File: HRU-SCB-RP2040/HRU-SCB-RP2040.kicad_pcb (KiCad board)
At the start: 2 copper layers, 42 x 55 mm, 52 parts, among them J1 Conn_01x03_Pin, J10 Conn_01x03_Pin, J11 Conn_01x03_Pin, J12 Conn_01x03_Pin, J13 Conn_01x03_Pin, J14 Conn_01x03_Pin, J15 Conn_01x03_Pin, J16 Conn_01x03_Pin, J17 Conn_01x03_Pin, J18 Conn_01x03_Pin, J19 Conn_01x03_Pin, J2 Conn_01x03_Pin, J20 Conn_01x03_Pin, J21 Conn_01x03_Pin, J22 Conn_01x03_Pin, J23 Conn_01x03_Pin, J24 Conn_01x03_Pin, J25 Conn_01x02_Pin, J26 Pico_Socket_A, J27 Pico_Socket_B, J28 Conn_01x04_Pin, J3 Conn_01x03_Pin, J4 Conn_01x03_Pin, J5 Conn_01x03_Pin, J6 Conn_01x03_Pin, J7 Conn_01x03_Pin, J8 Conn_01x03_Pin, J9 Conn_01x03_Pin, Q1 NchFET, Q2 NchFET, U2 MAX485E, U3 MAX485E, U4 NJM7805FA

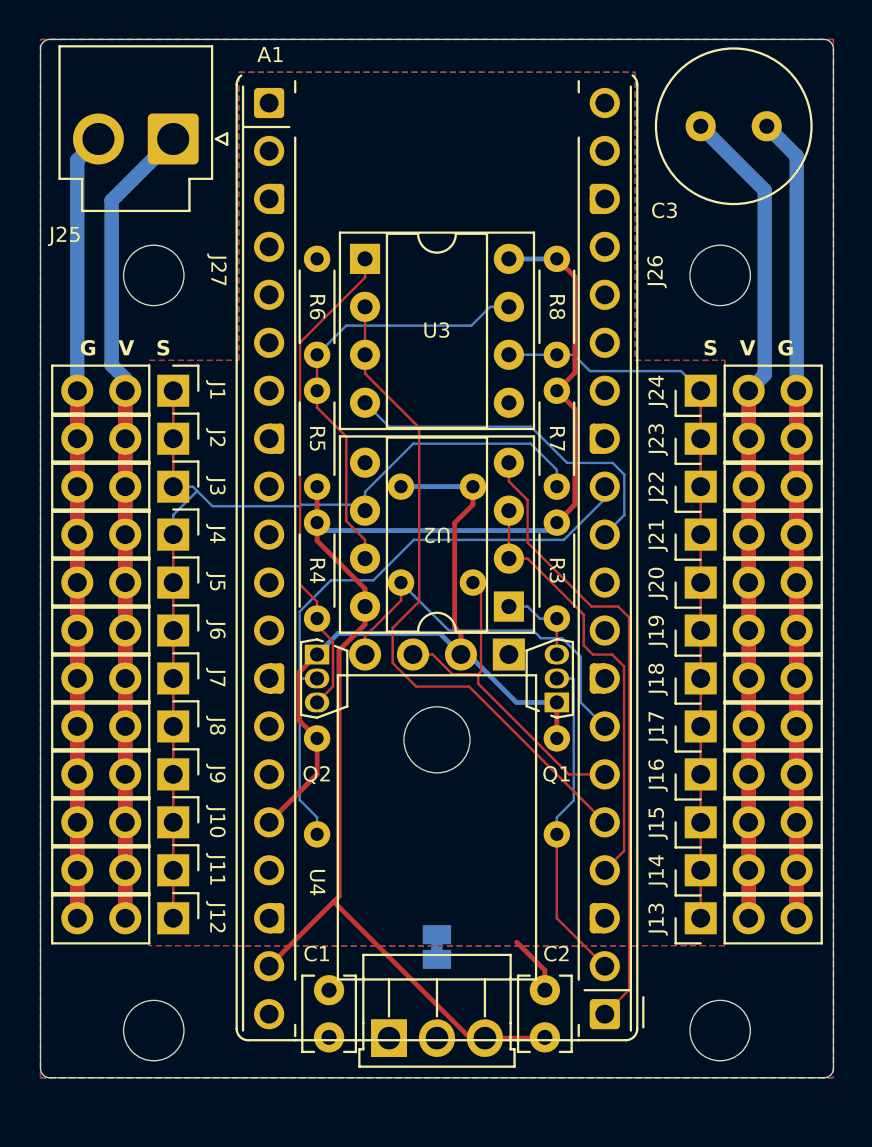
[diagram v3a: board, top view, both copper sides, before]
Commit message: Modify footprint of the registers and regulators
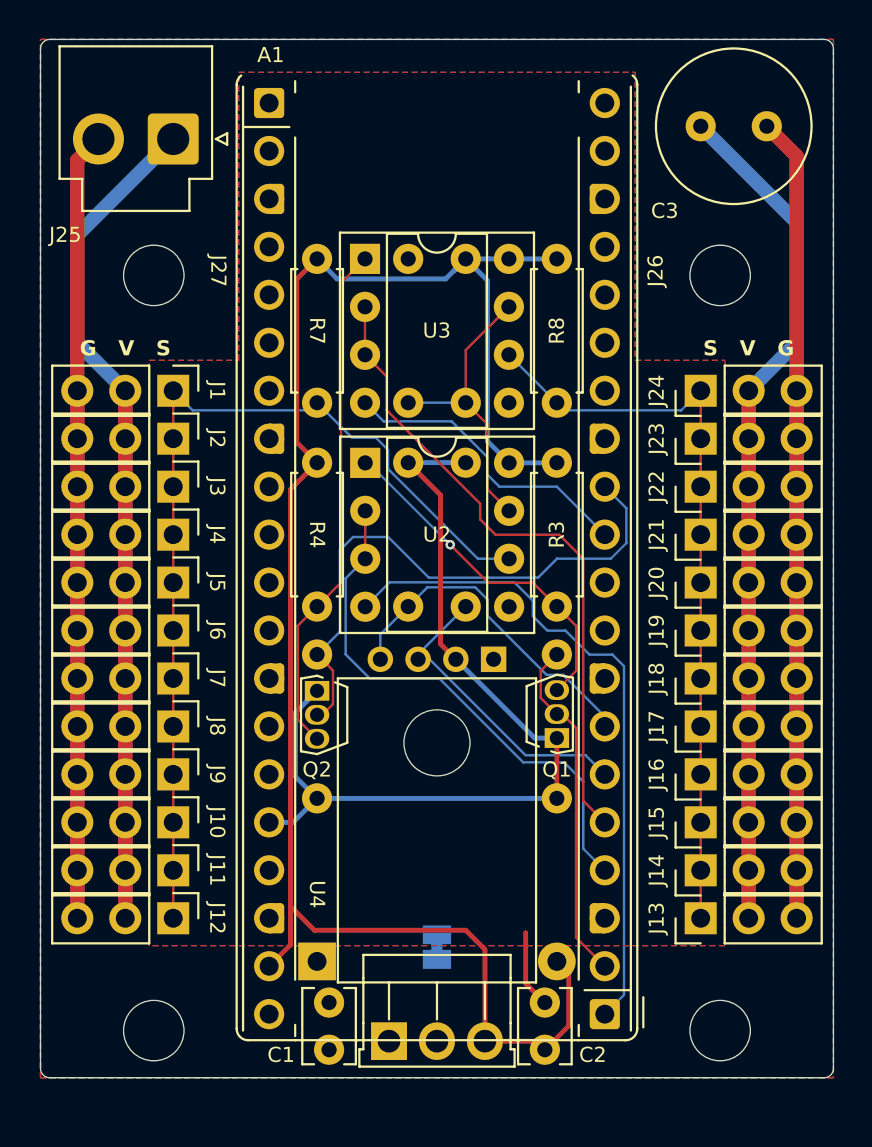
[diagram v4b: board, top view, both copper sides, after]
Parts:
- added D1: D_Small, Diode_THT:D_T-1_P12.70mm_Horizontal, B.Cu at (143.7, 143.8)
- added REF**: Symbol_CC-Attribution_CopperTop_Small, Symbol:Symbol_CC-Attribution_CopperTop_Small, B.Cu at (154.6, 138.8)
- J28: value Conn_01x04_Pin -> Conn_01x04_Socket; footprint mymod:PinHeader_1x04_P2.54mm_Vertical_SmallCourtyard -> Connector_PinHeader_2.00mm:PinHeader_1x04_P2.00mm_Vertical
- R1, R10, R2, R3, R4, R7, R8, R9: footprint Resistor_THT:R_Axial_DIN0204_L3.6mm_D1.6mm_P5.08mm_Horizontal -> Resistor_THT:R_Axial_DIN0207_L6.3mm_D2.5mm_P7.62mm_Horizontal
- R5, R6: footprint Resistor_THT:R_Axial_DIN0204_L3.6mm_D1.6mm_P5.08mm_Horizontal -> Resistor_THT:R_Axial_DIN0207_L6.3mm_D2.5mm_P7.62mm_Horizontal; moved to B.Cu
- moved R7 14.5 mm to (143.7, 106.6)
- moved R5 14.4 mm to (151.5, 106.6), turned to -90 degrees
- moved U2 10.8 mm to (146.2, 117.4), turned to 0 degrees
- moved R6 5.45 mm to (148.5, 114.2)
- moved R3 3.17 mm to (156.3, 117.4)
- moved R4 3.17 mm to (143.7, 117.4)
- moved R1 3.17 mm to (156.3, 135.2), turned to 90 degrees
- moved R2 3.17 mm to (143.7, 135.2), turned to 90 degrees
- moved Q2 1.92 mm to (143.7, 129.5)
- moved Q1 1.88 mm to (156.3, 132.0)
- moved R10 1.33 mm to (151.5, 125.0)
- moved R9 1.33 mm to (148.5, 125.0)
- moved J28 0.85 mm to (153.0, 127.8)
- moved C1 0.65 mm to (144.3, 148.5)
- moved C2 0.65 mm to (155.7, 148.5)
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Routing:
- net +5V: track 73.9 -> 93.1 mm
- net Net-(Q1-D): track 4.71 -> 18.6 mm, vias 0 -> 1
- net /ServoPort/SERVO.NULL: track 23.1 -> 15.8 mm
- net +3V3: track 40.5 -> 47.2 mm
- net /SERVO.SERIAL0.DE: track 23.2 -> 28.6 mm
- net VCC: track 142.5 -> 145.4 mm
- net /SERVO.SERIAL1.TX: track 18.9 -> 16.1 mm
- net /SERVO.SERIAL0.TX: track 33.2 -> 35.4 mm
- net /ServoPort/SERVO.SERIAL0: track 52.5 -> 50.3 mm
- net /I2C0.SDA: track 18.2 -> 16.3 mm
- net /I2C0.SCL: track 20.0 -> 18.1 mm
- net /SERVO.SERIAL1.RX: track 32.4 -> 30.7 mm
- net Net-(Q2-D): track 26.0 -> 27.3 mm
- net /SERVO.SERIAL0.RX: track 17.5 -> 18.4 mm
- net /ServoPort/SERVO.SERIAL1: track 38.9 -> 39.7 mm
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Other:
- board text added: "CC BY 4.0 UEC-RMF-HRU"

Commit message: update: circuit design of HRU-SCB-RP2040
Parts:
- removed D1: D_Small, Diode_THT:D_T-1_P12.70mm_Horizontal
- Q1, Q2: value NchFET -> BS170; footprint Package_TO_SOT_THT:TO-92S -> Package_TO_SOT_THT:TO-92_Inline_W4.0mm_Horizontal_FlatSideDown; moved to B.Cu
- R1, R2: moved to F.Cu
- R3: value 2.2k -> 5.1k; moved to B.Cu
- R4, R7, R8: moved to B.Cu
- U4: value NJM7805FA -> L7805
- moved R1 26.4 mm to (143.7, 112.1), turned to -90 degrees
- moved R2 26.4 mm to (156.3, 112.1), turned to -90 degrees
- moved Q2 13.6 mm to (157.1, 127.6), turned to 180 degrees
- moved Q1 11.8 mm to (145.4, 127.6), turned to 180 degrees
- moved R3 7.62 mm to (156.3, 125.0), turned to 90 degrees
- moved R4 7.62 mm to (143.7, 125.0), turned to 90 degrees
- moved R7 7.62 mm to (143.7, 114.2), turned to 90 degrees
- moved R8 7.62 mm to (156.3, 114.2), turned to 90 degrees
- moved REF** 2.54 mm to (154.6, 141.3)
- moved J28 0.25 mm to (153.0, 127.6)
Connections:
- Q1 pad 1: +3V3 -> Net-(Q1-D)
- Q1 pad 2: /SERVO.SERIAL0.RX -> +3V3
- Q1 pad 3: Net-(Q1-D) -> /SERVO.SERIAL0.RX
- Q2 pad 1: +3V3 -> Net-(Q2-D)
- Q2 pad 2: /SERVO.SERIAL1.RX -> +3V3
- Q2 pad 3: Net-(Q2-D) -> /SERVO.SERIAL1.RX
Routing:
- net VCC: track 145.4 -> 111.8 mm
- net GNDPWR: track 140.2 -> 111.8 mm
- net /SERVO.SERIAL0.RX: track 18.4 -> 37.7 mm, vias 0 -> 1
- net /SERVO.SERIAL1.RX: track 30.7 -> 13.5 mm
- net +3V3: track 47.2 -> 60.6 mm
- net /ServoPort/SERVO.SERIAL0: track 50.3 -> 59.8 mm
- net /SERVO.SERIAL1.DE: track 34.5 -> 42.4 mm, vias 0 -> 2
- net Net-(Q2-D): track 27.3 -> 34.0 mm
- net /ServoPort/SERVO.SERIAL1: track 39.7 -> 44.7 mm
- net /SERVO.SERIAL0.TX: track 35.4 -> 30.9 mm, vias 0 -> 1
- net /SERVO.SERIAL0.DE: track 28.6 -> 32.6 mm, vias 0 -> 1
- net /I2C0.SDA: track 16.3 -> 20.1 mm, vias 0 -> 1
- net Net-(Q1-D): track 18.6 -> 21.7 mm, vias 1 -> 0
- net +5V: track 93.1 -> 96.0 mm
- net /SERVO.SERIAL1.TX: track 16.1 -> 18.8 mm
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
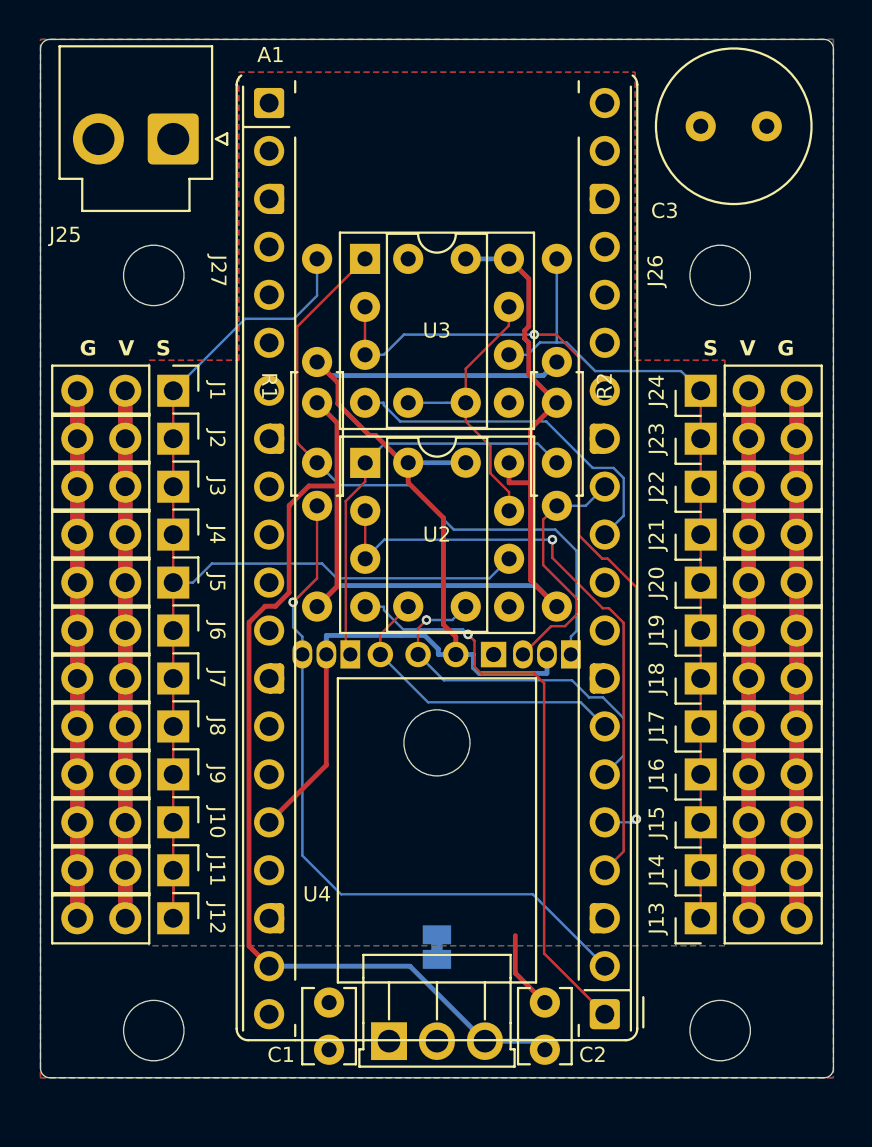
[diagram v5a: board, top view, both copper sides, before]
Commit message: Update: apply super DCDC
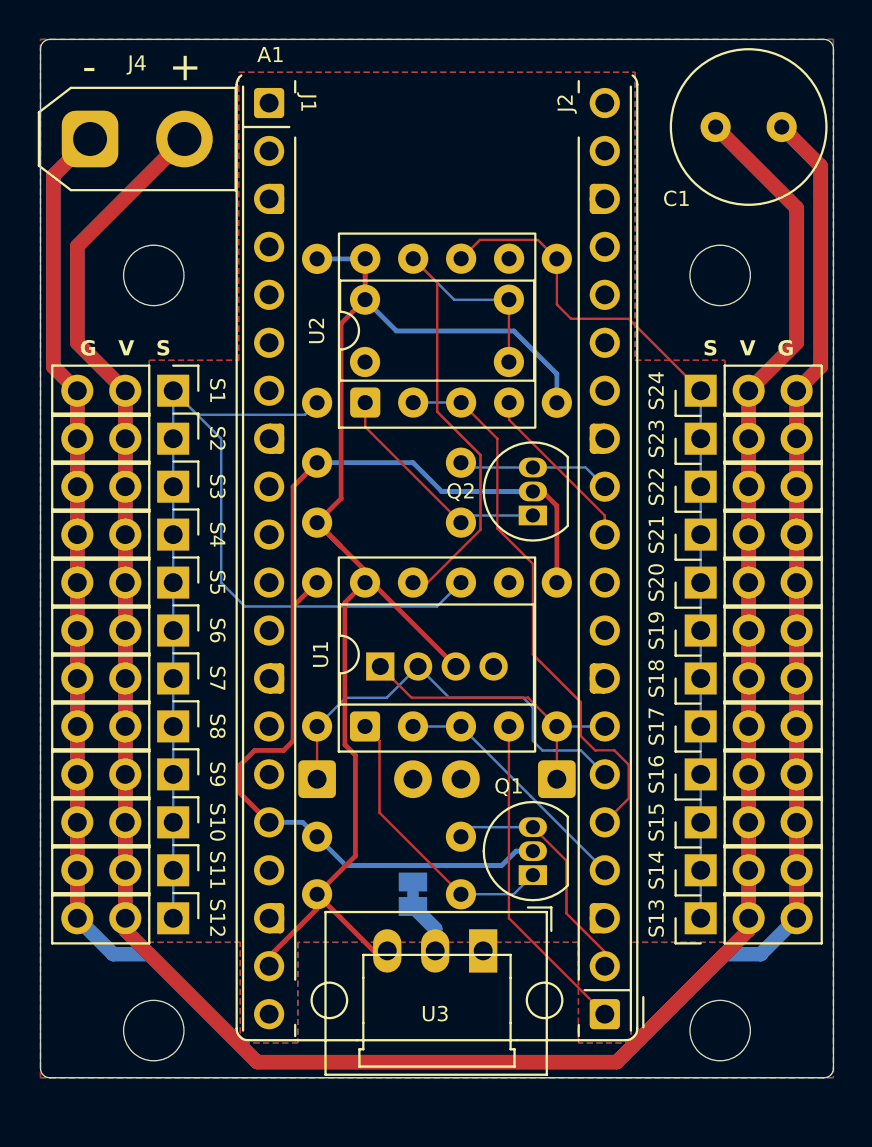
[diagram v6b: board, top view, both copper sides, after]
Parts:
- removed C2: 0.1uF, Capacitor_THT:C_Disc_D3.8mm_W2.6mm_P2.50mm
- removed C3: 220u, Capacitor_THT:C_Radial_D8.0mm_H11.5mm_P3.50mm
- removed J10, J11, J12, J13, J14, J15, J16, J17, J18, J19, J20, J21, J22, J23, J24, J5, J6, J7, J8, J9: Conn_01x03_Pin, mymod:PinHeader_1x03_P2.54mm_Vertical_SmallCourtyard
- removed J25: Conn_01x02_Pin, Connector_JST:JST_VH_B2P-VH_1x02_P3.96mm_Vertical
- removed J26: Pico_Socket_A, Module_RaspberryPi_Pico:RaspberryPi_Pico_PinSocket_1x20_P2.54mm_Vertical
- removed J27: Pico_Socket_B, Module_RaspberryPi_Pico:RaspberryPi_Pico_PinSocket_1x20_P2.54mm_Vertical
- removed J28: Conn_01x04_Socket, Connector_PinHeader_2.00mm:PinHeader_1x04_P2.00mm_Vertical
- removed U4: L7805, Package_TO_SOT_THT:TO-220F-3_Horizontal_TabDown
- added D1: D_Zener_Small, Diode_THT:D_T-1_P5.08mm_Horizontal, B.Cu at (156.3, 134.2)
- added D2: D_Zener_Small, Diode_THT:D_T-1_P5.08mm_Horizontal, B.Cu at (143.7, 134.2)
- added S1: Conn_01x03_Pin, mymod:PinHeader_1x03_P2.54mm_Vertical_SmallCourtyard, F.Cu at (136.0, 113.6)
- added S10: Conn_01x03_Pin, mymod:PinHeader_1x03_P2.54mm_Vertical_SmallCourtyard, F.Cu at (136.0, 136.5)
- added S11: Conn_01x03_Pin, mymod:PinHeader_1x03_P2.54mm_Vertical_SmallCourtyard, F.Cu at (136.0, 139.0)
- added S12: Conn_01x03_Pin, mymod:PinHeader_1x03_P2.54mm_Vertical_SmallCourtyard, F.Cu at (136.0, 141.6)
- added S13: Conn_01x03_Pin, mymod:PinHeader_1x03_P2.54mm_Vertical_SmallCourtyard, F.Cu at (164.0, 141.6)
- added S14: Conn_01x03_Pin, mymod:PinHeader_1x03_P2.54mm_Vertical_SmallCourtyard, F.Cu at (164.0, 139.0)
- added S15: Conn_01x03_Pin, mymod:PinHeader_1x03_P2.54mm_Vertical_SmallCourtyard, F.Cu at (164.0, 136.5)
- added S16: Conn_01x03_Pin, mymod:PinHeader_1x03_P2.54mm_Vertical_SmallCourtyard, F.Cu at (164.0, 133.9)
- added S17: Conn_01x03_Pin, mymod:PinHeader_1x03_P2.54mm_Vertical_SmallCourtyard, F.Cu at (164.0, 131.4)
- added S18: Conn_01x03_Pin, mymod:PinHeader_1x03_P2.54mm_Vertical_SmallCourtyard, F.Cu at (164.0, 128.8)
- added S19: Conn_01x03_Pin, mymod:PinHeader_1x03_P2.54mm_Vertical_SmallCourtyard, F.Cu at (164.0, 126.3)
- added S2: Conn_01x03_Pin, mymod:PinHeader_1x03_P2.54mm_Vertical_SmallCourtyard, F.Cu at (136.0, 116.2)
- added S20: Conn_01x03_Pin, mymod:PinHeader_1x03_P2.54mm_Vertical_SmallCourtyard, F.Cu at (164.0, 123.8)
- added S21: Conn_01x03_Pin, mymod:PinHeader_1x03_P2.54mm_Vertical_SmallCourtyard, F.Cu at (164.0, 121.2)
- added S22: Conn_01x03_Pin, mymod:PinHeader_1x03_P2.54mm_Vertical_SmallCourtyard, F.Cu at (164.0, 118.7)
- added S23: Conn_01x03_Pin, mymod:PinHeader_1x03_P2.54mm_Vertical_SmallCourtyard, F.Cu at (164.0, 116.2)
- added S24: Conn_01x03_Pin, mymod:PinHeader_1x03_P2.54mm_Vertical_SmallCourtyard, F.Cu at (164.0, 113.6)
- added S3: Conn_01x03_Pin, mymod:PinHeader_1x03_P2.54mm_Vertical_SmallCourtyard, F.Cu at (136.0, 118.7)
- added S4: Conn_01x03_Pin, mymod:PinHeader_1x03_P2.54mm_Vertical_SmallCourtyard, F.Cu at (136.0, 121.2)
- added S5: Conn_01x03_Pin, mymod:PinHeader_1x03_P2.54mm_Vertical_SmallCourtyard, F.Cu at (136.0, 123.8)
- added S6: Conn_01x03_Pin, mymod:PinHeader_1x03_P2.54mm_Vertical_SmallCourtyard, F.Cu at (136.0, 126.3)
- added S7: Conn_01x03_Pin, mymod:PinHeader_1x03_P2.54mm_Vertical_SmallCourtyard, F.Cu at (136.0, 128.8)
- added S8: Conn_01x03_Pin, mymod:PinHeader_1x03_P2.54mm_Vertical_SmallCourtyard, F.Cu at (136.0, 131.4)
- added S9: Conn_01x03_Pin, mymod:PinHeader_1x03_P2.54mm_Vertical_SmallCourtyard, F.Cu at (136.0, 133.9)
- added U1: MAX485E, Package_DIP:DIP-8_W7.62mm_Socket, F.Cu at (146.2, 131.4)
- C1: value 0.33uF -> 220u; footprint Capacitor_THT:C_Disc_D3.8mm_W2.6mm_P2.50mm -> Capacitor_THT:C_Radial_D8.0mm_H11.5mm_P3.50mm
- J1: value Conn_01x03_Pin -> Pico_Socket_B; footprint mymod:PinHeader_1x03_P2.54mm_Vertical_SmallCourtyard -> Module_RaspberryPi_Pico:RaspberryPi_Pico_PinSocket_1x20_P2.54mm_Vertical
- J2: value Conn_01x03_Pin -> Pico_Socket_A; footprint mymod:PinHeader_1x03_P2.54mm_Vertical_SmallCourtyard -> Module_RaspberryPi_Pico:RaspberryPi_Pico_PinSocket_1x20_P2.54mm_Vertical
- J3: value Conn_01x03_Pin -> GROVE-CONNECTOR-DIP_4P-2.0_; footprint mymod:PinHeader_1x03_P2.54mm_Vertical_SmallCourtyard -> OPL_Connector:GROVE-HW4-2.0; moved to B.Cu
- J4: value Conn_01x03_Pin -> Conn_01x02_Pin; footprint mymod:PinHeader_1x03_P2.54mm_Vertical_SmallCourtyard -> Connector_AMASS:AMASS_XT30UPB-M_1x02_P5.0mm_Vertical
- Q1, Q2: footprint Package_TO_SOT_THT:TO-92_Inline_W4.0mm_Horizontal_FlatSideDown -> Package_TO_SOT_THT:TO-92_Inline; moved to F.Cu
- R1, R2: value 5.1k -> 2.2k; moved to B.Cu
- R7, R8: value 2.2k -> 5.1k
- U3: value MAX485E -> R-78E3.3-0.5; footprint Package_DIP:DIP-8_W7.62mm_Socket -> Converter_DCDC:Converter_DCDC_RECOM_R-78E-0.5_THT
- moved C1 53.0 mm to (164.8, 99.6), turned to 0 degrees
- moved J2 38.1 mm to (158.9, 146.6), turned to 180 degrees
- moved U3 37.2 mm to (152.4, 143.3), turned to 180 degrees
- moved R5 34.6 mm to (143.7, 140.3), turned to 0 degrees
- moved R1 23.1 mm to (156.3, 131.4), turned to 90 degrees
- moved R2 23.1 mm to (143.7, 131.4), turned to 90 degrees
- moved J4 21.4 mm to (131.6, 100.3), turned to 0 degrees
- moved R9 19.0 mm to (143.7, 106.6), turned to -90 degrees
- moved R3 17.6 mm to (143.7, 137.2), turned to 0 degrees
- moved J3 16.9 mm to (150.0, 128.2), turned to 0 degrees
- moved J1 16.1 mm to (141.1, 98.4), turned to 0 degrees
- moved Q1 15.2 mm to (155.1, 139.3), turned to 90 degrees
- moved R10 11.8 mm to (156.3, 114.2)
- moved R6 7.98 mm to (143.7, 120.6), turned to 0 degrees
- moved Q2 7.63 mm to (155.1, 120.2), turned to 90 degrees
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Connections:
- J1 pad 1: /ServoPort/SERVO.SERIAL0 -> unconnected-(J1-GPIO16-Pad1)
- J1 pad 2: VCC -> unconnected-(J1-GPIO17-Pad2)
- J1 pad 3: GNDPWR -> GND
- J2 pad 1: /ServoPort/SERVO.SERIAL0 -> /SERVO.SERIAL0.TX
- J2 pad 2: VCC -> /SERVO.SERIAL0.RX
- J2 pad 3: GNDPWR -> GND
- J3 pad 1: /ServoPort/SERVO.SERIAL0 -> /I2C0.SCL
- J3 pad 2: VCC -> /I2C0.SDA
- J3 pad 3: GNDPWR -> +5V
- J4 pad 1: /ServoPort/SERVO.SERIAL0 -> GNDPWR
- R1 pad 1: +3V3 -> /I2C0.SCL
- R1 pad 2: /SERVO.SERIAL0.RX -> +3V3
- R10 pad 1: /I2C0.SDA -> +5V
- R10 pad 2: +3V3 -> /ServoPort/SERVO.SERIAL1
- R2 pad 1: +3V3 -> /I2C0.SDA
- R2 pad 2: /SERVO.SERIAL1.RX -> +3V3
- R3 pad 1: +5V -> +3V3
- R3 pad 2: Net-(Q1-D) -> /SERVO.SERIAL0.RX
- R4 pad 1: +5V -> +3V3
- R4 pad 2: Net-(Q2-D) -> /SERVO.SERIAL1.RX
- R5 pad 2: /ServoPort/SERVO.NULL -> Net-(Q1-D)
- R6 pad 1: /ServoPort/SERVO.NULL -> +5V
- R6 pad 2: GND -> Net-(Q2-D)
- R7 pad 2: /ServoPort/SERVO.SERIAL0 -> /ServoPort/SERVO.NULL
- R8 pad 1: +5V -> /ServoPort/SERVO.NULL
- R8 pad 2: /ServoPort/SERVO.SERIAL1 -> GND
- R9 pad 1: /I2C0.SCL -> +5V
- R9 pad 2: +3V3 -> /ServoPort/SERVO.SERIAL0
- U2 pad 1: Net-(Q1-D) -> Net-(Q2-D)
- U2 pad 2: /SERVO.SERIAL0.DE -> /SERVO.SERIAL1.DE
- U2 pad 3: /SERVO.SERIAL0.DE -> /SERVO.SERIAL1.DE
- U2 pad 4: /SERVO.SERIAL0.TX -> /SERVO.SERIAL1.TX
- U2 pad 6: /ServoPort/SERVO.SERIAL0 -> /ServoPort/SERVO.SERIAL1
- U3 pad 1: Net-(Q2-D) -> VCC
- U3 pad 2: /SERVO.SERIAL1.DE -> GNDPWR
- U3 pad 3: /SERVO.SERIAL1.DE -> +5V
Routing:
- net GNDPWR: track 111.8 -> 219.0 mm
- net VCC: track 111.8 -> 218.9 mm
- net /SERVO.SERIAL0.RX: track 37.7 -> 13.0 mm, vias 1 -> 0
- net +5V: track 96.0 -> 71.4 mm
- net Net-(Q2-D): track 34.0 -> 12.4 mm
- net /SERVO.SERIAL0.DE: track 32.6 -> 13.3 mm, vias 1 -> 0
- net /ServoPort/SERVO.NULL: track 15.8 -> 29.8 mm
- net /SERVO.SERIAL0.TX: track 30.9 -> 17.3 mm, vias 1 -> 0
- net /SERVO.SERIAL1.DE: track 42.4 -> 29.6 mm, vias 2 -> 0
- net /SERVO.SERIAL1.TX: track 18.8 -> 9.10 mm
- net Net-(Q1-D): track 21.7 -> 15.2 mm
- net /SERVO.SERIAL1.RX: track 13.5 -> 8.15 mm
- net GND: track 4.19 -> 0.00 mm
- net +3V3: track 60.6 -> 57.0 mm
- net /I2C0.SDA: track 20.1 -> 22.8 mm, vias 1 -> 0
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
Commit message: fix(HRU-SCB-RP2040): add diodes for level shift
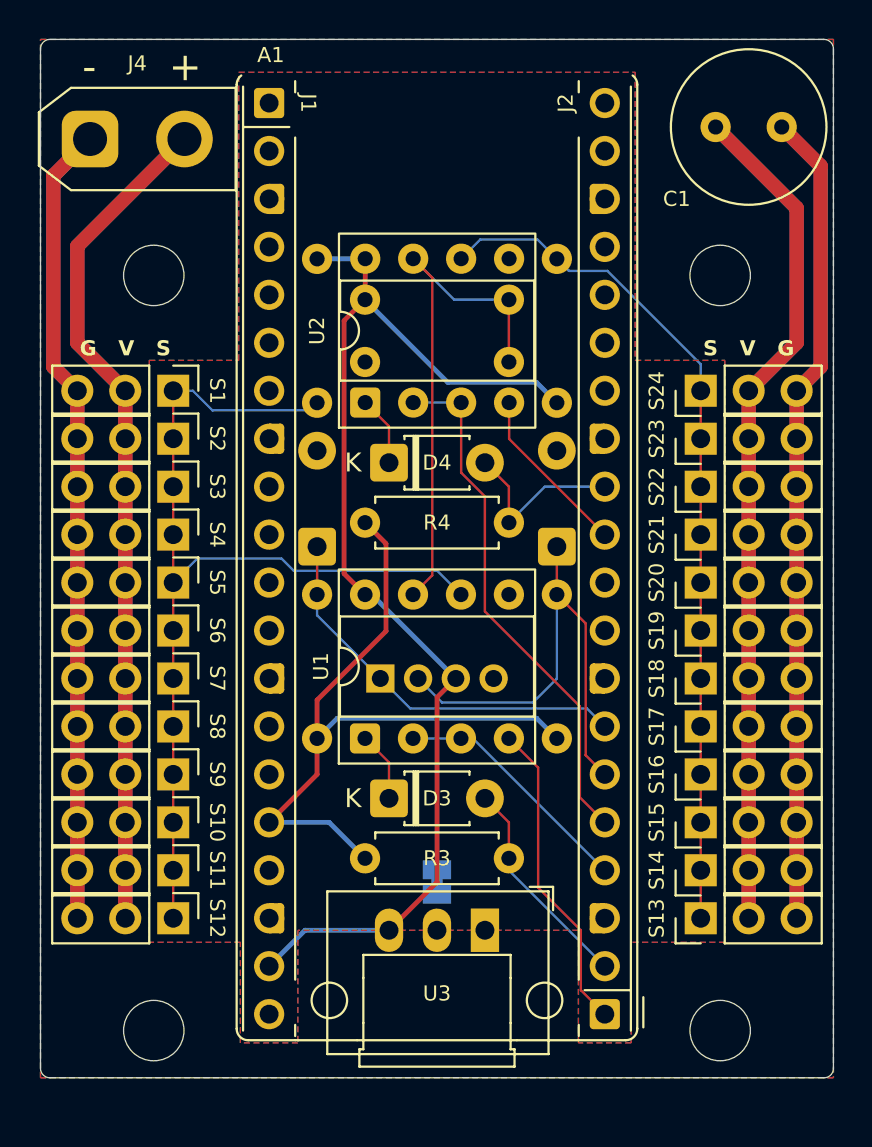
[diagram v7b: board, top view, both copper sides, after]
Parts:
- removed Q1, Q2: BS170, Package_TO_SOT_THT:TO-92_Inline
- removed R5, R6: 5.1k, Resistor_THT:R_Axial_DIN0207_L6.3mm_D2.5mm_P7.62mm_Horizontal
- added D3: 1N4148, Diode_THT:D_T-1_P5.08mm_Horizontal, F.Cu at (147.5, 135.2)
- added D4: 1N4148, Diode_THT:D_T-1_P5.08mm_Horizontal, F.Cu at (147.5, 117.4)
- D1, D2: value D_Zener_Small -> D_Zener_3V3
- R3, R4: moved to F.Cu
- moved D1 17.7 mm to (143.7, 121.9), turned to 90 degrees
- moved D2 17.7 mm to (156.3, 121.9), turned to 90 degrees
- moved R1 14.5 mm to (143.7, 124.4), turned to -90 degrees
- moved R2 14.5 mm to (156.3, 124.4), turned to -90 degrees
- moved R4 4.07 mm to (146.2, 120.6)
- moved R3 2.79 mm to (146.2, 138.4)
- moved JP1 1.43 mm to (150.0, 139.6)
- moved U3 1.10 mm to (152.5, 142.2)
- moved U1 0.64 mm to (146.2, 132.0)
- moved J3 0.63 mm to (150.0, 128.8)
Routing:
- net GNDPWR: track 219.0 -> 171.8 mm
- net VCC: track 218.9 -> 178.8 mm
- net +3V3: track 57.0 -> 38.3 mm
- net Net-(D3-K): track 15.2 -> 3.70 mm
- net +5V: track 71.4 -> 62.3 mm
- net Net-(D4-K): track 12.4 -> 3.71 mm
- net /ServoPort/SERVO.SERIAL0: track 59.5 -> 52.7 mm
- net /I2C0.SCL: track 16.0 -> 21.3 mm
- net /I2C0.SDA: track 22.8 -> 26.0 mm
- net /ServoPort/SERVO.NULL: track 29.8 -> 27.9 mm
- net /SERVO.SERIAL1.DE: track 29.6 -> 27.9 mm
- net /SERVO.SERIAL0.RX: track 13.0 -> 11.5 mm
- net /SERVO.SERIAL1.RX: track 8.15 -> 9.57 mm
- net /SERVO.SERIAL0.TX: track 17.3 -> 16.7 mm
- net /ServoPort/SERVO.SERIAL1: track 45.8 -> 45.2 mm
